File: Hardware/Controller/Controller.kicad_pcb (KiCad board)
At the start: 2 copper layers, 35 x 124 mm, 60 parts, among them J1 8P8C, J2 LCD Header, J3 USB_B_Micro, J4 S88, J5 Screw_Terminal_01x05, SW1 Rotary_Encoder_Switch, SW2 SW_F0, SW3 SW_F1, SW4 SW_F2, SW5 SW_F3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

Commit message: Optimizations
* Moved Screen connector to the other side
* Optimized knee bends
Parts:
- J2: moved to B.Cu
- moved J2 7.49 mm to (35.4, 49.7)
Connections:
- U1 pad 11: /I2C_SDA -> /I2C_SCL
- U1 pad 12: /I2C_SCL -> /I2C_SDA
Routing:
- net GND: track 497.1 -> 492.2 mm, vias 23 -> 32
- net VCC: track 252.8 -> 255.6 mm, vias 6 -> 5
- net /I2C_SDA: track 13.0 -> 11.4 mm
- net /I2C_SCL: track 10.4 -> 11.7 mm
- net /Stop: track 31.1 -> 30.1 mm
- net /GPIO0: track 24.2 -> 23.5 mm
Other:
- board text added: "SDA SCL VCC GND"
- board text removed: "GND VCC SCL SDA"

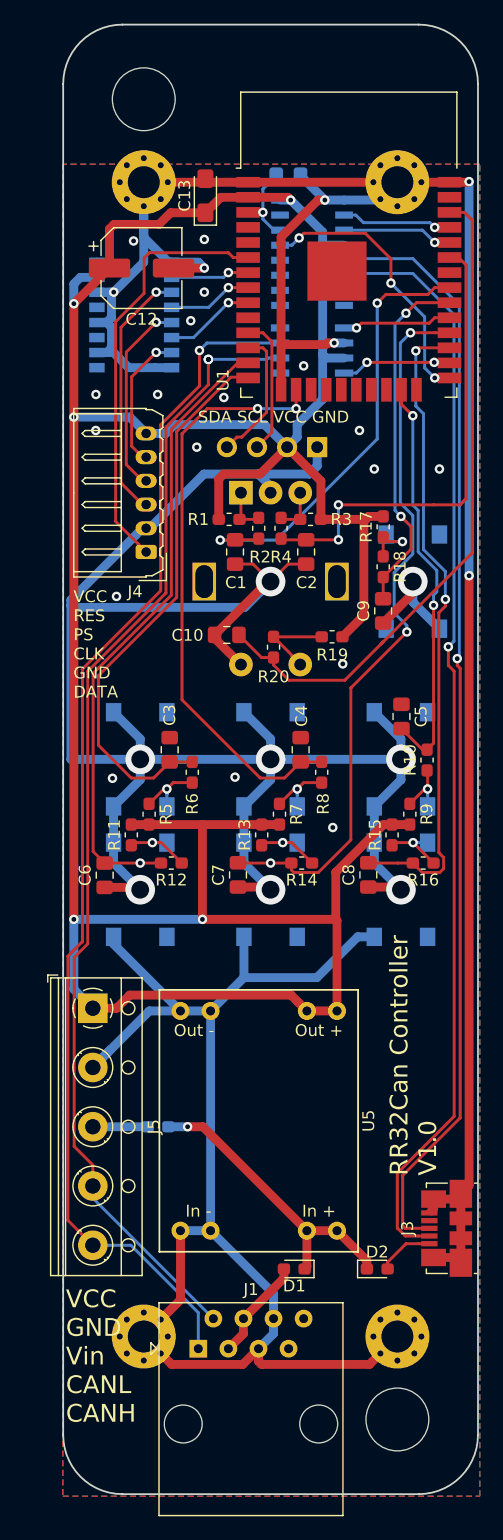
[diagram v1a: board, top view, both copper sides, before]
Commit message: Fixed part footprints
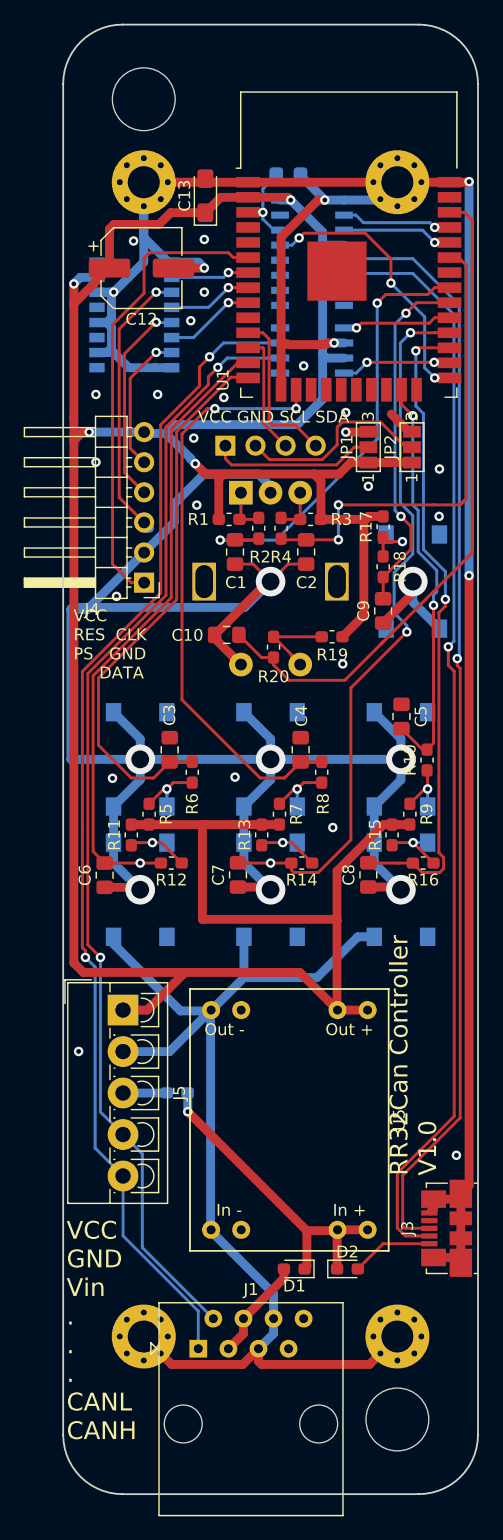
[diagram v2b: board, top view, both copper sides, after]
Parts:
- added JP1: PIN1, Jumper:SolderJumper-3_P1.3mm_Open_Pad1.0x1.5mm_NumberLabels, F.Cu at (39.8, 49.7)
- added JP2: PIN2, Jumper:SolderJumper-3_P1.3mm_Open_Pad1.0x1.5mm_NumberLabels, F.Cu at (43.4, 49.7)
- J4: footprint Connector_Molex:Molex_Micro-Latch_53254-0670_1x06_P2.00mm_Horizontal -> Connector_PinHeader_2.54mm:PinHeader_1x06_P2.54mm_Horizontal
- J5: footprint TerminalBlock_RND:TerminalBlock_RND_205-00015_1x05_P5.00mm_Horizontal -> TerminalBlock_4Ucon:TerminalBlock_4Ucon_1x05_P3.50mm_Vertical
- moved J2 7.75 mm to (27.7, 49.5), turned to 270 degrees
- moved D3 3.29 mm to (23.6, 104.1)
- moved J4 2.59 mm to (20.8, 61.1), turned to 180 degrees
- moved U5 2.58 mm to (33.1, 106.4)
- moved J5 2.55 mm to (19.1, 97.2)
- moved D2 2.51 mm to (38.0, 119.0)
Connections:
- J2 pad 1: GND -> Net-(J2-Pad1)
- J2 pad 2: VCC -> Net-(J2-Pad2)
- J2 pad 3: /I2C_SCL -> /I2C_SDA
- J2 pad 4: /I2C_SDA -> /I2C_SCL
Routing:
- net GND: track 492.2 -> 474.6 mm, vias 32 -> 37
- net Net-(J2-Pad2): track 0.00 -> 16.8 mm
- net Net-(J2-Pad1): track 0.00 -> 14.0 mm
- net VCC: track 255.6 -> 260.9 mm, vias 5 -> 4
- net /CANH: track 102.4 -> 98.9 mm, vias 1 -> 2
- net /S88_DATA: track 36.0 -> 39.4 mm
- net /VinUsb: track 4.74 -> 6.91 mm
- net /VinCommon: track 25.4 -> 27.5 mm
- net /CANL: track 96.8 -> 94.8 mm
- net /I2C_SCL: track 11.7 -> 13.7 mm
- net /S88_CLOCK: track 21.5 -> 23.5 mm
- net /I2C_SDA: track 11.4 -> 10.3 mm
- net /VinTerminal: track 4.62 -> 3.70 mm
- net /S88_PS: track 16.6 -> 17.5 mm
- net /S88_RESET: track 11.7 -> 12.3 mm
- removed copper zone on B.Cu, net GND
- removed copper zone on F.Cu, net GND
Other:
- board text added: "VCC GND SCL SDA"
- board text added: "VCC GND Vin . . . CANL CANH"
- board text added: "VCC RES CLK PS GND DATA"
- board text removed: "SDA SCL VCC GND"
- board text removed: "VCC GND Vin CANL CANH"
- board text removed: "VCC RES PS CLK GND DATA"

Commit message: Fixes for Manufacturing
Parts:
- removed D3: D_Schottky, Diode_SMD:D_0603_1608Metric_Pad1.05x0.95mm_HandSolder
- moved D1 6.45 mm to (36.3, 113.2)
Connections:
- J5 pad 3: /VinTerminal -> /VinCAN
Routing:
- net /VinCAN: track 8.67 -> 35.7 mm
- net /VinCommon: track 27.5 -> 8.38 mm, vias 1 -> 0
- net /VinTerminal: track 3.70 -> 0.00 mm
- net GND: vias 37 -> 39
- added copper zone on B.Cu, net GND
- added copper zone on F.Cu, net GND
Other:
- board text added: "JP1 JP2 SCL SDA"
- board text added: "RR32Can V1.0 Controller"
- board text added: "VCC GND Vin CANL CANH"
- board text added: "VCC RES PS CLK GND DATA"
- board text removed: "RR32Can Controller V1.0"
- board text removed: "VCC GND SCL SDA"
- board text removed: "VCC GND Vin . . . CANL CANH"
- board text removed: "VCC RES CLK PS GND DATA"

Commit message: Swap RX/TX
Fixes #1
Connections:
- U1 pad 34: /RX0 -> /BOARD_RX0
- U1 pad 35: /TX0 -> /BOARD_TX0
- U4 pad 2: /TX0 -> /BOARD_RX0
- U4 pad 3: /RX0 -> /BOARD_TX0
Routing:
- net /BOARD_RX0: track 0.00 -> 9.88 mm, vias 0 -> 1
- net /TX0: track 9.47 -> 0.00 mm, vias 1 -> 0
- net /RX0: track 9.47 -> 0.00 mm, vias 1 -> 0
- net /BOARD_TX0: track 0.00 -> 9.32 mm, vias 0 -> 1
- net /Stop: track 30.1 -> 30.7 mm
- net GND: vias 39 -> 40
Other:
- board text added: "RR32Can V1.1 Controller"
- board text removed: "RR32Can V1.0 Controller"
